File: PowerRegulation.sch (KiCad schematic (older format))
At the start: 6 parts, among them U301 LM2931

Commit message: updated schematic capacitor symbols to use new default library symbols
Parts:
- C301, C302: Fieldname (none) -> Value
- R301, R302, R303: symbol R -> R-RESCUE-CurrentSinkOrSwim
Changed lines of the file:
@@
 EESchema Schematic File Version 2
+LIBS:CurrentSinkOrSwim-rescue
 LIBS:power
 LIBS:device
@@
 LIBS:memory
 LIBS:xilinx
-LIBS:special
 LIBS:microcontrollers
 LIBS:dsp
@@
 $EndComp
 $Comp
-L C C301
-U 1 1 54DAF10D
-P 4000 3300
-F 0 "C301" H 4050 3400 50  0000 L CNN
-F 1 ".1" H 4050 3200 50  0000 L CNN
-F 2 "SMD_Packages:SMD-0805" H 4038 3150 30  0001 C CNN
-F 3 "" H 4000 3300 60  0000 C CNN
-	1    4000 3300
-	-1   0    0    -1
-$EndComp
-$Comp
-L C C302
-U 1 1 54DAF114
-P 6200 3450
-F 0 "C302" H 6250 3550 50  0000 L CNN
-F 1 ".1" H 6250 3350 50  0000 L CNN
-F 2 "SMD_Packages:SMD-0805" H 6238 3300 30  0001 C CNN
-F 3 "" H 6200 3450 60  0000 C CNN
-	1    6200 3450
-	-1   0    0    -1
-$EndComp
-Wire Wire Line
-	4000 3800 4000 3500
-$Comp
-L R R301
+L R-RESCUE-CurrentSinkOrSwim R301
 U 1 1 54DAF11D
 P 4200 3200
@@
 Connection ~ 6200 2650
 $Comp
-L R R302
+L R-RESCUE-CurrentSinkOrSwim R302
 U 1 1 54DAF13B
 P 5650 2950
@@
 $EndComp
 $Comp
-L R R303
+L R-RESCUE-CurrentSinkOrSwim R303
 U 1 1 54DAF142
 P 5650 3550
@@
 	5650 3850 5650 3800
 Connection ~ 4800 3850
-Wire Wire Line
-	6200 3850 6200 3650
 Connection ~ 5650 3850
 Wire Wire Line
@@
 Wire Wire Line
 	5650 3200 5650 3300
+$Comp
+L C C302
+U 1 1 57B0CCA3
+P 6200 3400
+F 0 "C302" H 6225 3500 50  0000 L CNN
+F 1 ".1" H 6225 3300 50  0000 L CNN
+F 2 "SMD_Packages:SMD-0805" H 6238 3250 50  0001 C CNN
+F 3 "" H 6200 3400 50  0000 C CNN
+F 4 "Value" H 6200 3400 60  0001 C CNN "Fieldname"
+	1    6200 3400
+	-1   0    0    -1
+$EndComp
+Wire Wire Line
+	6200 3850 6200 3550
+$Comp
+L C C301
+U 1 1 57B0D032
+P 4000 3250
+F 0 "C301" H 4025 3350 50  0000 L CNN
+F 1 ".1" H 4025 3150 50  0000 L CNN
+F 2 "SMD_Packages:SMD-0805" H 4038 3100 50  0001 C CNN
+F 3 "" H 4000 3250 50  0000 C CNN
+F 4 "Value" H 4000 3250 60  0001 C CNN "Fieldname"
+	1    4000 3250
+	-1   0    0    -1
+$EndComp
+Wire Wire Line
+	4000 3400 4000 3800
 $EndSCHEMATC

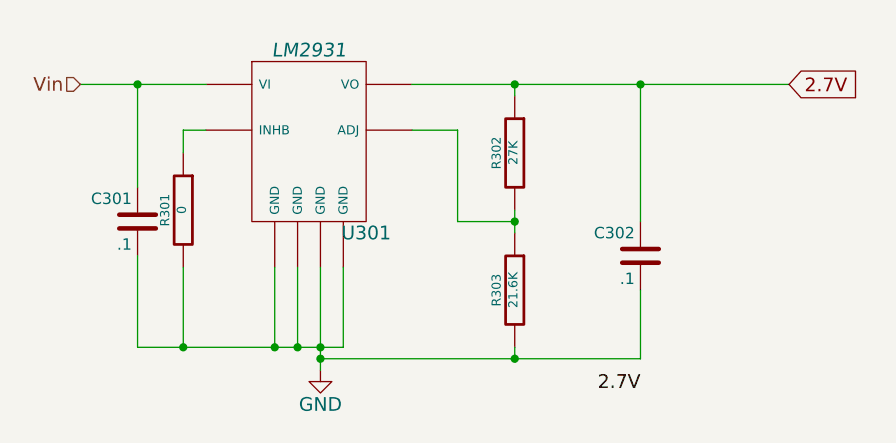
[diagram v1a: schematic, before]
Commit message: corrected cap on voltage regulator and corrected voltage divider in voltage control
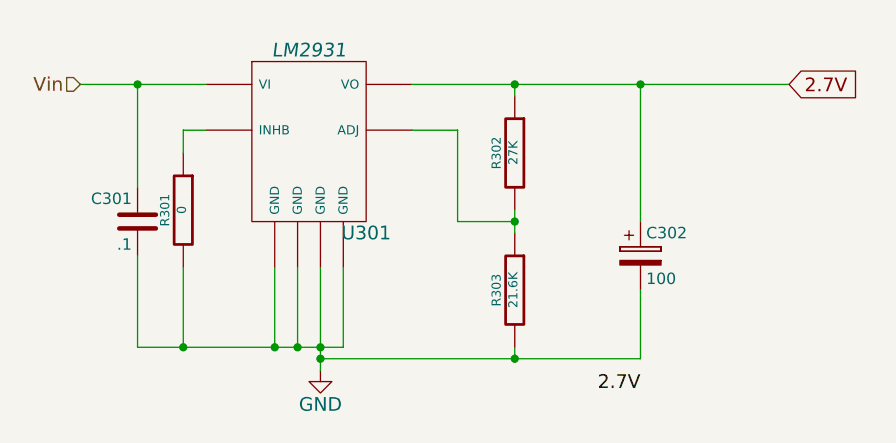
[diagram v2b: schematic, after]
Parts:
- removed C302: .1, SMD_Packages:SMD-0805, symbol C
- added C302: 100, symbol CP
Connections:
- net 2.7V: now also C302.1
- net GND: now also C302.2
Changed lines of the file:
@@
 EESchema Schematic File Version 2
-LIBS:CurrentSinkOrSwim-rescue
 LIBS:power
 LIBS:device
@@
 Wire Wire Line
 	5650 3200 5650 3300
-$Comp
-L C C302
-U 1 1 57B0CCA3
-P 6200 3400
-F 0 "C302" H 6225 3500 50  0000 L CNN
-F 1 ".1" H 6225 3300 50  0000 L CNN
-F 2 "SMD_Packages:SMD-0805" H 6238 3250 50  0001 C CNN
-F 3 "" H 6200 3400 50  0000 C CNN
-F 4 "Value" H 6200 3400 60  0001 C CNN "Fieldname"
-	1    6200 3400
-	-1   0    0    -1
-$EndComp
 Wire Wire Line
 	6200 3850 6200 3550
@@
 Wire Wire Line
 	4000 3400 4000 3800
+$Comp
+L CP C302
+U 1 1 57B34636
+P 6200 3400
+F 0 "C302" H 6225 3500 50  0000 L CNN
+F 1 "100" H 6225 3300 50  0000 L CNN
+F 2 "" H 6238 3250 50  0000 C CNN
+F 3 "" H 6200 3400 50  0000 C CNN
+F 4 "Value" H 6200 3400 60  0001 C CNN "Fieldname"
+	1    6200 3400
+	1    0    0    -1
+$EndComp
 $EndSCHEMATC

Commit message: updated diode to sod-323 package and used new schematic symbol because pin numbers changed
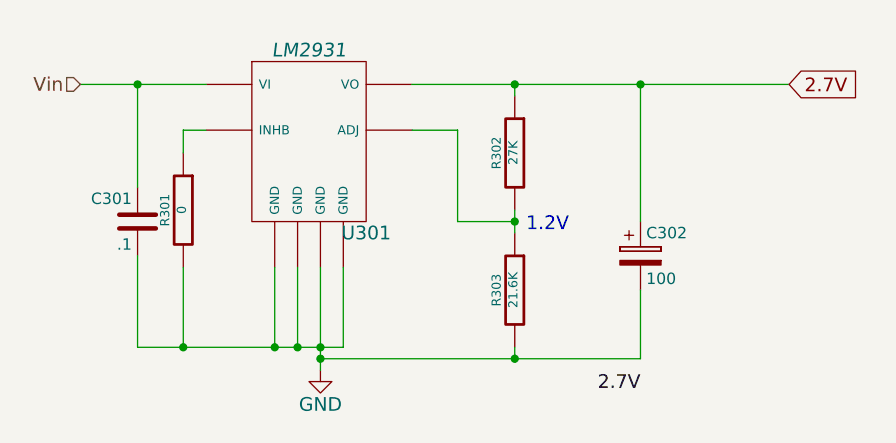
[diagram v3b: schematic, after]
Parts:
- C302: MPN (none) -> PCE3867CT-ND
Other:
- note added: "1.2V\n"
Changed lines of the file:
@@
 F 3 "" H 6200 3400 50  0000 C CNN
 F 4 "Value" H 6200 3400 60  0001 C CNN "Fieldname"
+F 5 "PCE3867CT-ND" H 6200 3400 60  0001 C CNN "MPN"
 	1    6200 3400
 	1    0    0    -1
 $EndComp
+Text Notes 5700 3300 0    60   ~ 0
+1.2V\n
 $EndSCHEMATC
